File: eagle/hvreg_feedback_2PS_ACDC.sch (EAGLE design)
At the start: 20 parts

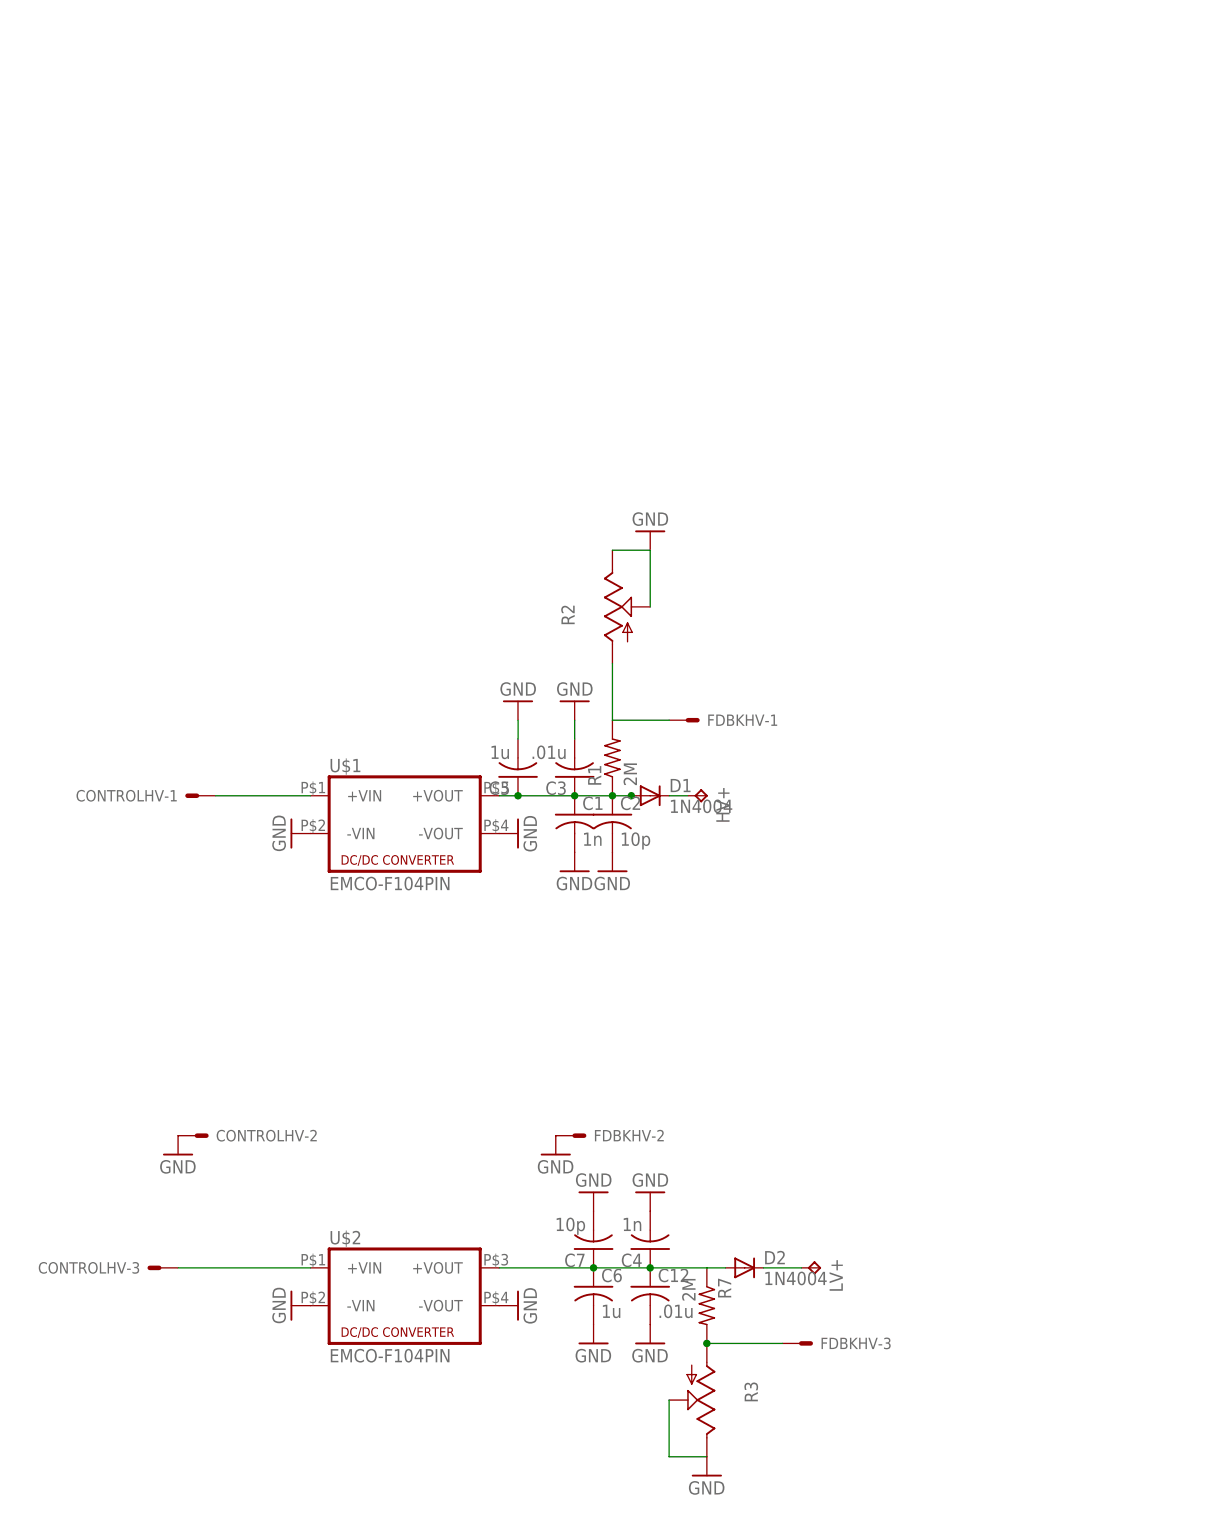
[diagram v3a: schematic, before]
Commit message: update for thermal issues and CTIA breakout
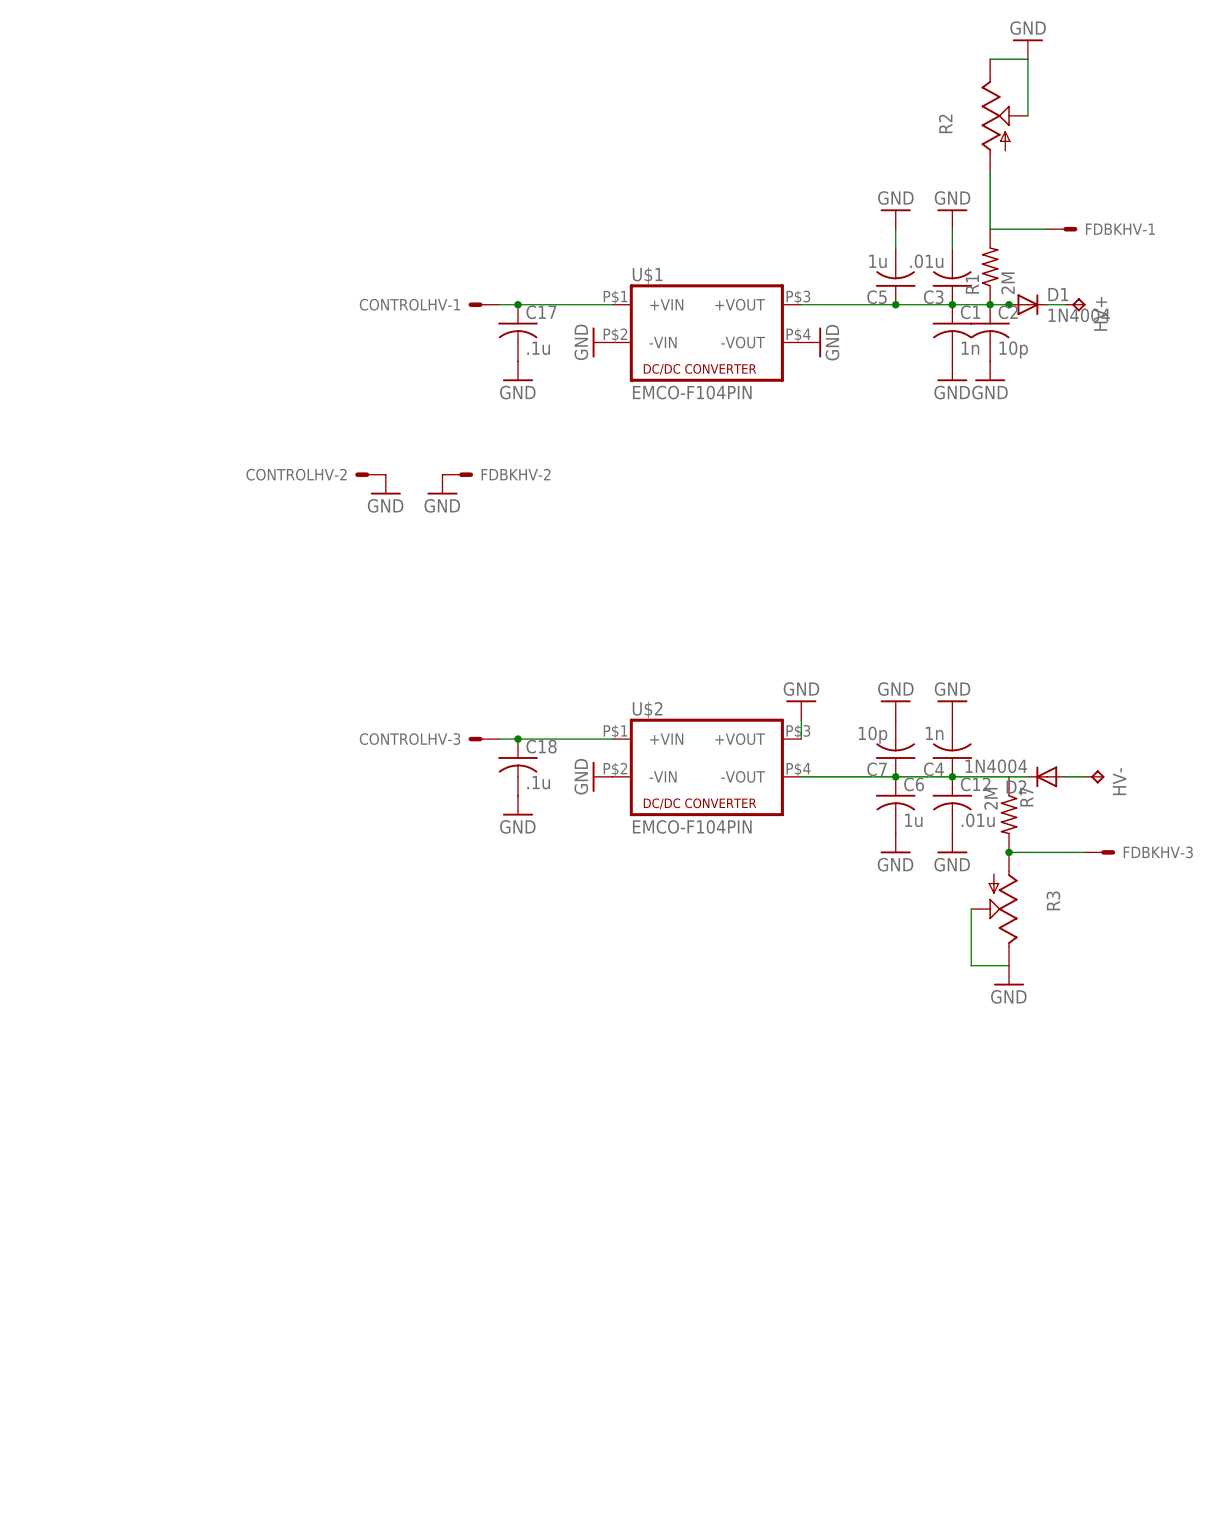
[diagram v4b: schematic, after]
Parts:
- removed LV+: TPPAD1-20Y, testpad:TPPAD1-20Y
- added C17, C18: .1u, rcl:C-US225-113X268
- added HV-: TPPAD1-20Y, testpad:TPPAD1-20Y
- C1, C12, C2, C3, C4, C7: device rcl:C-US075-042X103 -> rcl:C-US102-043X133
- R1, R7: device resistor:R-US_0207/12 -> resistor:R-US_0613/15
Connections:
- removed net N$5: CONTROLHV-3.S, U$2.+VIN
- removed net N$7: D2.C, LV+.TP
- new net N$13: C17.1, CONTROLHV-1.S, U$1.+VIN
- new net N$15: C18.1, CONTROLHV-3.S, U$2.+VIN
- net GND: now also C17.2, C18.2, U$2.+VOUT; no longer U$2.-VOUT
- net N$2: now also D2.C, U$2.-VOUT; no longer D2.A, U$2.+VOUT
- net N$4: now also D2.A, HV-.TP; no longer CONTROLHV-1.S, U$1.+VIN
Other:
- moved on the sheet: C1, C12, C2, C3, C4, C5, C6, C7, CONTROLHV-1, CONTROLHV-2, CONTROLHV-3, D1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
